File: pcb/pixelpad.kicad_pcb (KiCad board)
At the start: 2 copper layers, 100 x 60.1 mm, 27 parts, among them SW1 SW_Push, SW10 SW_Push, SW11 SW_Push, SW12 SW_Push, SW2 SW_Push, SW3 SW_Push, SW4 RotaryEncoder_Switch, SW5 SW_Push, SW6 SW_Push, SW7 SW_Push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

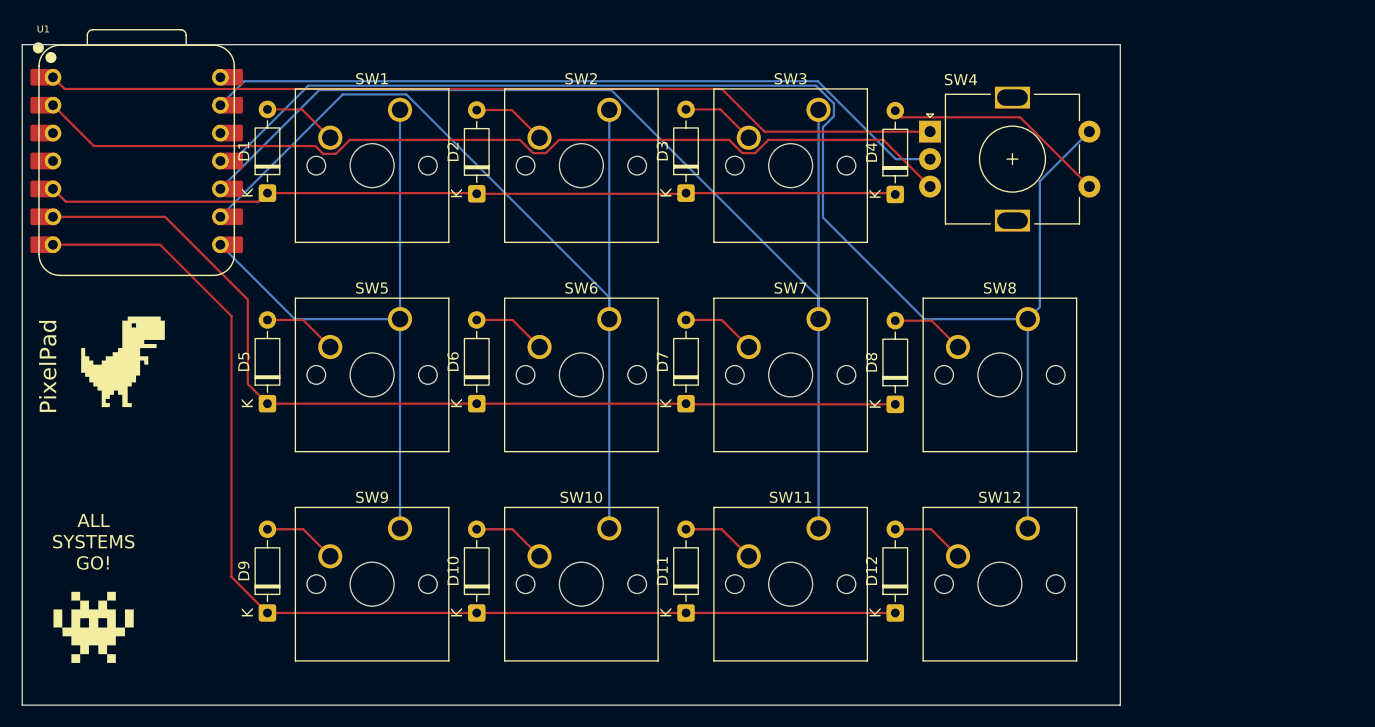
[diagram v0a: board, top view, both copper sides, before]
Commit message: added sw_push, moved rotary encoder to bottom right, mcu to top right
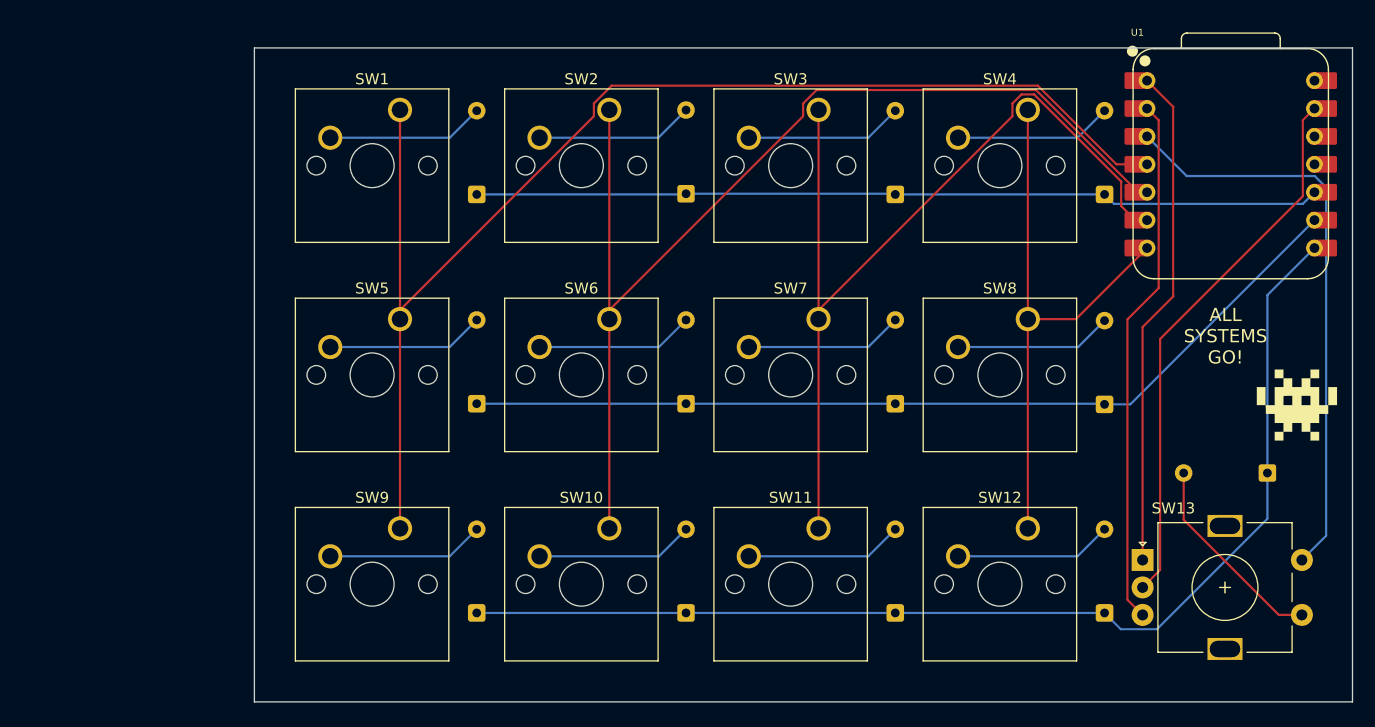
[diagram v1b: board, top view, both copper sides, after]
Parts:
- added D4: 1N4148WT, Diode_THT:D_DO-35_SOD27_P7.62mm_Horizontal, B.Cu at (161.9, 36.0)
- added SW4: SW_Push, Button_Switch_Keyboard:SW_Cherry_MX_1.00u_PCB, F.Cu at (154.9, 28.3)
- D1, D10, D11, D12, D2, D3, D5, D6, D7, D8, D9, G***: moved to B.Cu
- D13: renamed from D4; moved to B.Cu
- moved G*** 111.4 mm to (179.5, 55.1)
- moved U1 99.6 mm to (173.4, 33.2)
- moved SW13 43.5 mm to (165.4, 69.2)
- moved D13 42.3 mm to (176.7, 61.3), turned to 180 degrees
- moved G*** 32.7 mm to (92.3, 77.4), turned to 180 degrees
- moved D1 19.1 mm to (104.8, 36.0)
- moved D3 19.1 mm to (142.9, 36.0)
- moved D12 19.0 mm to (161.9, 74.1)
- moved D8 19.0 mm to (161.9, 55.1)
- moved D10 19.0 mm to (123.8, 74.1)
- moved D11 19.0 mm to (142.9, 74.1)
- moved D5 19.0 mm to (104.8, 55.0)
- moved D6 19.0 mm to (123.8, 55.0)
- moved D7 19.0 mm to (142.9, 55.0)
- moved D9 19.0 mm to (104.8, 74.1)
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- renumbered SW4 to SW13
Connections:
- D13 pad 1: ROW0 -> ROW2
- SW13 pad S2: COL3 -> ENC_SWB
- U1 pad 10: COL2 -> ROW0
- U1 pad 11: COL3 -> unconnected-(U1-GPIO3/MOSI-Pad11)
- U1 pad 3: unconnected-(U1-GPIO28/ADC2/A2-Pad3) -> ENC_SWB
- U1 pad 4: unconnected-(U1-GPIO29/ADC3/A3-Pad4) -> COL0
- U1 pad 5: ROW0 -> COL1
- U1 pad 6: ROW1 -> COL2
- U1 pad 7: ROW2 -> COL3
- U1 pad 8: COL0 -> ROW2
- U1 pad 9: COL1 -> ROW1
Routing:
- net COL3: track 131.1 -> 51.6 mm
- net COL0: track 57.3 -> 119.0 mm
- net ENC_SWB: track 0.00 -> 53.1 mm
- net ENC_B: track 86.0 -> 48.3 mm
- net ENC_A: track 81.9 -> 45.8 mm
- net COL2: track 106.1 -> 83.7 mm
- net GND: track 68.4 -> 50.1 mm
- net Net-(D4-A): track 0.00 -> 14.4 mm
- net COL1: track 87.7 -> 100.7 mm
- net Net-(D2-A): track 6.76 -> 14.4 mm
- net Net-(D5-A): track 6.73 -> 14.4 mm
- net Net-(D9-A): track 6.73 -> 14.4 mm
- net Net-(D6-A): track 6.73 -> 14.4 mm
- net Net-(D10-A): track 6.73 -> 14.4 mm
- net Net-(D7-A): track 6.73 -> 14.4 mm
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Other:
- board size 100 x 60.1 mm -> 100 x 59.5 mm
